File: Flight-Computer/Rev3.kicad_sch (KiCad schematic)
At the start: 2 parts, among them P11 440054-3, U14 MX25V5126FM1I

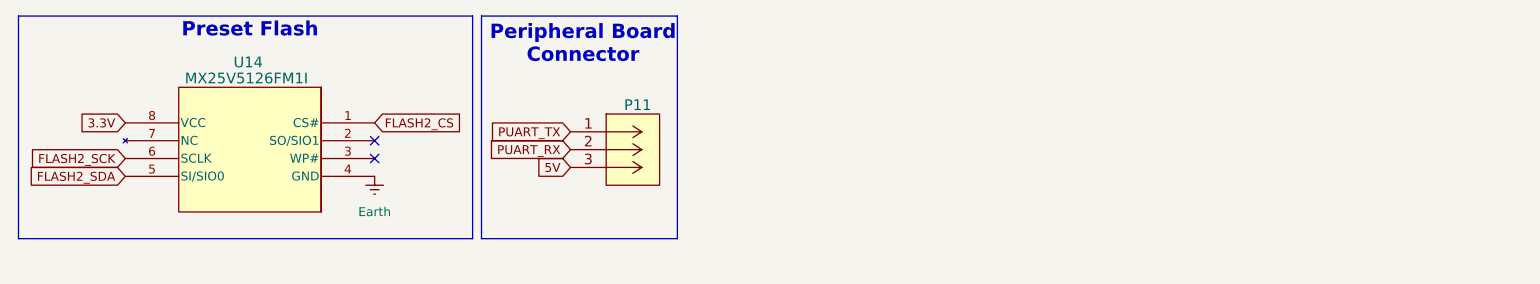
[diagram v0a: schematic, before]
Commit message: New Flash/4x UART
Added Microchip Technologies Flash and 3 more UART peripheral connectors
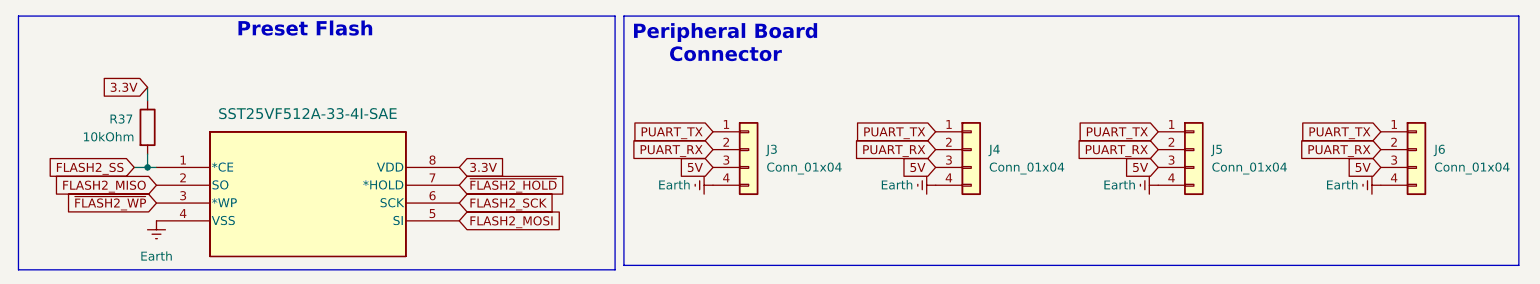
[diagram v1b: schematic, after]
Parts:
- removed P11: 440054-3, Flight-Computer:440054-3, symbol Flight-Computer:440054-3
- removed U14: MX25V5126FM1I, 8-SOP_MX25V_M1_MAC, symbol MX25V5126FM1I:MX25V5126FM1I
- added J3, J4, J5, J6: Conn_01x04, Connector_JST:JST_PH_B4B-PH-K_1x04_P2.00mm_Vertical, symbol Connector_Generic:Conn_01x04
- added R37: 10kOhm, symbol Device:R
- added U15: SST25VF512A-33-4I-SAE, SOIC8_SA_SST_MCH, symbol SST25VF512A-33-4I-SAE:SST25VF512A-33-4I-SAE
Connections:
- net 3.3V: now also R37.1, U15.8 (VDD)
- net 5V: now also J3.3 (Pin_3), J4.3 (Pin_3), J5.3 (Pin_3), J6.3 (Pin_3)
- net Earth: now also J3.4 (Pin_4), J4.4 (Pin_4), J5.4 (Pin_4), J6.4 (Pin_4), U15.4 (VSS)
- net FLASH2_SCK: now also U15.6 (SCK)
- net PUART_RX: now also J3.2 (Pin_2), J4.2 (Pin_2), J5.2 (Pin_2), J6.2 (Pin_2)
- net PUART_TX: now also J3.1 (Pin_1), J4.1 (Pin_1), J5.1 (Pin_1), J6.1 (Pin_1)
- new net FLASH2_MISO: U15.2 (SO)
- new net FLASH2_MOSI: U15.5 (SI)
- new net FLASH2_SS: R37.2, U15.1 (*CE)
- new net ~{FLASH2_HOLD}: U15.7 (*HOLD)
- new net ~{FLASH2_WP}: U15.3 (*WP)
- no-connect marks 2 -> 0

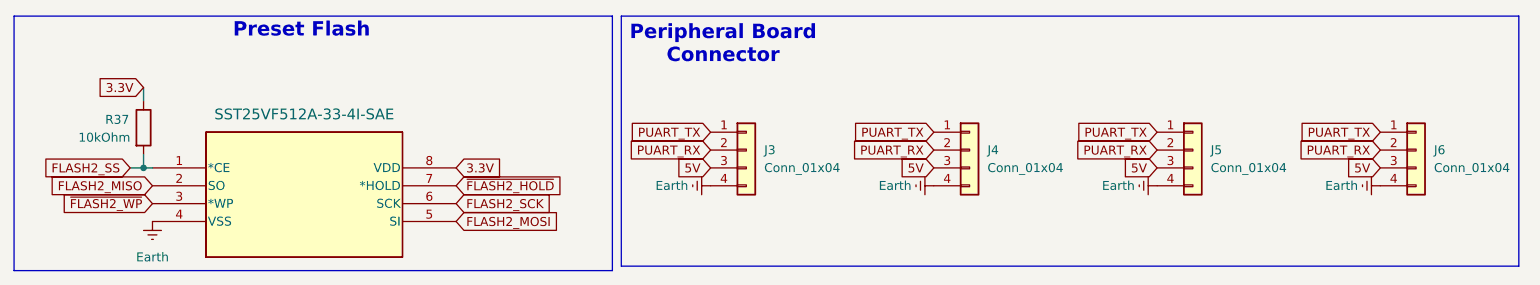
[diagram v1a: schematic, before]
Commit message: American PFLASH/PUART
Made to appease the American mind (Changed symbols and orientations)
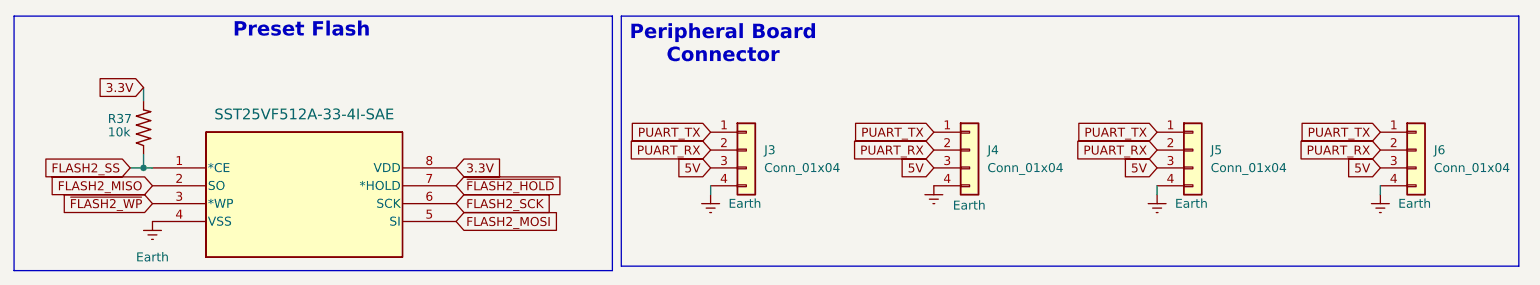
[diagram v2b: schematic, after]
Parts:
- removed R37: 10kOhm, symbol Device:R
- added R37: 10k, symbol Flight-Computer-Mac:RES_0603
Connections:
- net 3.3V: now also R37.2
- net FLASH2_SS: now also R37.1
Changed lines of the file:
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@@
+	(wire
+		(pts
+			(xy 111.76 38.1) (xy 111.76 36.83)
+		)
+		(stroke
+			(width 0)
+			(type default)
+		)
+	)
+	(wire
+		(pts
+			(xy 175.26 38.1) (xy 175.26 36.83)
+		)
+		(stroke
+			(width 0)
+			(type default)
+		)
+	)
 	(wire
 		(pts
@@
 		(pts
 			(xy 31.115 22.86) (xy 31.115 24.765)
+		)
+		(stroke
+			(width 0)
+			(type default)
+		)
+	)
+	(wire
+		(pts
+			(xy 207.01 38.1) (xy 207.01 36.83)
 		)
 		(stroke
@@
 	(symbol
 		(lib_id "power:Earth")
-		(at 175.26 36.83 270)
+		(at 175.26 38.1 0)
 		(unit 1)
 		(exclude_from_sim no)
@@
 		(fields_autoplaced yes)
 		(property "Reference" "#PWR067"
-			(at 168.91 36.83 0)
+			(at 175.26 44.45 0)
 			(effects
 				(font
@@
 		)
 		(property "Value" "Earth"
-			(at 172.085 36.8299 90)
-			(effects
-				(font
-					(size 1.27 1.27)
-				)
-				(justify right)
+			(at 177.8 39.3699 0)
+			(effects
+				(font
+					(size 1.27 1.27)
+				)
+				(justify left)
 			)
 		)
 		(property "Footprint" ""
-			(at 175.26 36.83 0)
+			(at 175.26 38.1 0)
 			(effects
 				(font
@@
 		)
 		(property "Datasheet" "~"
-			(at 175.26 36.83 0)
+			(at 175.26 38.1 0)
 			(effects
 				(font
@@
 		)
 		(property "Description" "Power symbol creates a global label with name \"Earth\""
-			(at 175.26 36.83 0)
+			(at 175.26 38.1 0)
 			(effects
 				(font
@@
 				(path "/15d2e012-e166-422c-a8f3-0484b565dd65/50820f75-73df-40b2-8569-4bcf15d0fdea"
 					(reference "#PWR067")
-					(unit 1)
-				)
-			)
-		)
-	)
-	(symbol
-		(lib_id "Device:R")
-		(at 31.115 28.575 0)
-		(unit 1)
-		(exclude_from_sim no)
-		(in_bom yes)
-		(on_board yes)
-		(dnp no)
-		(property "Reference" "R37"
-			(at 25.654 27.432 0)
-			(effects
-				(font
-					(size 1.27 1.27)
-				)
-				(justify left)
-			)
-		)
-		(property "Value" "10kOhm"
-			(at 21.844 29.972 0)
-			(effects
-				(font
-					(size 1.27 1.27)
-				)
-				(justify left)
-			)
-		)
-		(property "Footprint" ""
-			(at 29.337 28.575 90)
-			(effects
-				(font
-					(size 1.27 1.27)
-				)
-				(hide yes)
-			)
-		)
-		(property "Datasheet" "~"
-			(at 31.115 28.575 0)
-			(effects
-				(font
-					(size 1.27 1.27)
-				)
-				(hide yes)
-			)
-		)
-		(property "Description" "Resistor"
-			(at 31.115 28.575 0)
-			(effects
-				(font
-					(size 1.27 1.27)
-				)
-				(hide yes)
-			)
-		)
-		(pin "2"
-		)
-		(pin "1"
-		)
-		(instances
-			(project ""
-				(path "/15d2e012-e166-422c-a8f3-0484b565dd65/50820f75-73df-40b2-8569-4bcf15d0fdea"
-					(reference "R37")
 					(unit 1)
 				)
@@
 	(symbol
 		(lib_id "power:Earth")
-		(at 111.76 36.83 270)
+		(at 111.76 38.1 0)
 		(unit 1)
 		(exclude_from_sim no)
@@
 		(fields_autoplaced yes)
 		(property "Reference" "#PWR065"
-			(at 105.41 36.83 0)
+			(at 111.76 44.45 0)
 			(effects
 				(font
@@
 		)
 		(property "Value" "Earth"
-			(at 108.585 36.8299 90)
-			(effects
-				(font
-					(size 1.27 1.27)
-				)
-				(justify right)
+			(at 114.3 39.3699 0)
+			(effects
+				(font
+					(size 1.27 1.27)
+				)
+				(justify left)
 			)
 		)
 		(property "Footprint" ""
-			(at 111.76 36.83 0)
+			(at 111.76 38.1 0)
 			(effects
 				(font
@@
 		)
 		(property "Datasheet" "~"
-			(at 111.76 36.83 0)
+			(at 111.76 38.1 0)
 			(effects
 				(font
@@
 		)
 		(property "Description" "Power symbol creates a global label with name \"Earth\""
-			(at 111.76 36.83 0)
+			(at 111.76 38.1 0)
 			(effects
 				(font
@@
 				(path "/15d2e012-e166-422c-a8f3-0484b565dd65/50820f75-73df-40b2-8569-4bcf15d0fdea"
 					(reference "#PWR065")
+					(unit 1)
+				)
+			)
+		)
+	)
+	(symbol
+		(lib_id "Flight-Computer-Mac:RES_0603")
+		(at 31.115 28.575 90)
+		(unit 1)
+		(exclude_from_sim no)
+		(in_bom yes)
+		(on_board yes)
+		(dnp no)
+		(property "Reference" "R37"
+			(at 26.035 27.305 90)
+			(effects
+				(font
+					(size 1.27 1.27)
+				)
+				(justify right)
+			)
+		)
+		(property "Value" "10k"
+			(at 26.035 29.21 90)
+			(effects
+				(font
+					(size 1.27 1.27)
+				)
+				(justify right)
+			)
+		)
+		(property "Footprint" ""
+			(at 43.815 27.305 0)
+			(effects
+				(font
+					(size 1.27 1.27)
+				)
+				(justify left bottom)
+				(hide yes)
+			)
+		)
+		(property "Datasheet" ""
+			(at 31.115 28.575 0)
+			(effects
+				(font
+					(size 1.27 1.27)
+				)
+				(justify left bottom)
+				(hide yes)
+			)
+		)
+		(property "Description" ""
+			(at 31.115 28.575 0)
+			(effects
+				(font
+					(size 1.27 1.27)
+				)
+				(hide yes)
+			)
+		)
+		(pin "1"
+		)
+		(pin "2"
+		)
+		(instances
+			(project ""
+				(path "/15d2e012-e166-422c-a8f3-0484b565dd65/50820f75-73df-40b2-8569-4bcf15d0fdea"
+					(reference "R37")
 					(unit 1)
 				)
@@
 	(symbol
 		(lib_id "power:Earth")
-		(at 207.01 36.83 270)
+		(at 207.01 38.1 0)
 		(unit 1)
 		(exclude_from_sim no)
@@
 		(fields_autoplaced yes)
 		(property "Reference" "#PWR068"
-			(at 200.66 36.83 0)
+			(at 207.01 44.45 0)
 			(effects
 				(font
@@
 		)
 		(property "Value" "Earth"
-			(at 203.835 36.8299 90)
-			(effects
-				(font
-					(size 1.27 1.27)
-				)
-				(justify right)
+			(at 209.55 39.3699 0)
+			(effects
+				(font
+					(size 1.27 1.27)
+				)
+				(justify left)
 			)
 		)
 		(property "Footprint" ""
-			(at 207.01 36.83 0)
+			(at 207.01 38.1 0)
 			(effects
 				(font
@@
 		)
 		(property "Datasheet" "~"
-			(at 207.01 36.83 0)
+			(at 207.01 38.1 0)
 			(effects
 				(font
@@
 		)
 		(property "Description" "Power symbol creates a global label with name \"Earth\""
-			(at 207.01 36.83 0)
+			(at 207.01 38.1 0)
 			(effects
 				(font
@@
 	(symbol
 		(lib_id "power:Earth")
-		(at 143.51 36.83 270)
+		(at 143.51 36.83 0)
 		(unit 1)
 		(exclude_from_sim no)
@@
 		(on_board yes)
 		(dnp no)
-		(fields_autoplaced yes)
 		(property "Reference" "#PWR066"
-			(at 137.16 36.83 0)
+			(at 143.51 43.18 0)
 			(effects
 				(font
@@
 		)
 		(property "Value" "Earth"
-			(at 140.335 36.8299 90)
-			(effects
-				(font
+			(at 150.876 39.624 0)
+			(effects
+				(font

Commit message: Update Rev3.kicad_sch
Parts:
- removed R37: 10k, symbol Flight-Computer-Mac:RES_0603
- added R37: 10k, Flight-Computer:RES_0603, symbol Flight-Computer:RES_0603
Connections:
- net 3.3V: now also R37.2
- net FLASH2_SS: now also R37.1
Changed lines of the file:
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@@
 	)
 	(symbol
-		(lib_id "Flight-Computer-Mac:RES_0603")
+		(lib_id "Flight-Computer:RES_0603")
 		(at 31.115 28.575 90)
 		(unit 1)
@@
 		(on_board yes)
 		(dnp no)
+		(fields_autoplaced yes)
 		(property "Reference" "R37"
-			(at 26.035 27.305 90)
+			(at 32.8676 27.7403 90)
 			(effects
 				(font
@@
 		)
 		(property "Value" "10k"
-			(at 26.035 29.21 90)
+			(at 32.8676 30.2772 90)
 			(effects
 				(font
@@
 			)
 		)
-		(property "Footprint" ""
+		(property "Footprint" "Flight-Computer:RES_0603"
 			(at 43.815 27.305 0)
 			(effects
@@
 		)
 		(instances
-			(project ""
+			(project "Flight-Computer"
 				(path "/15d2e012-e166-422c-a8f3-0484b565dd65/50820f75-73df-40b2-8569-4bcf15d0fdea"
 					(reference "R37")

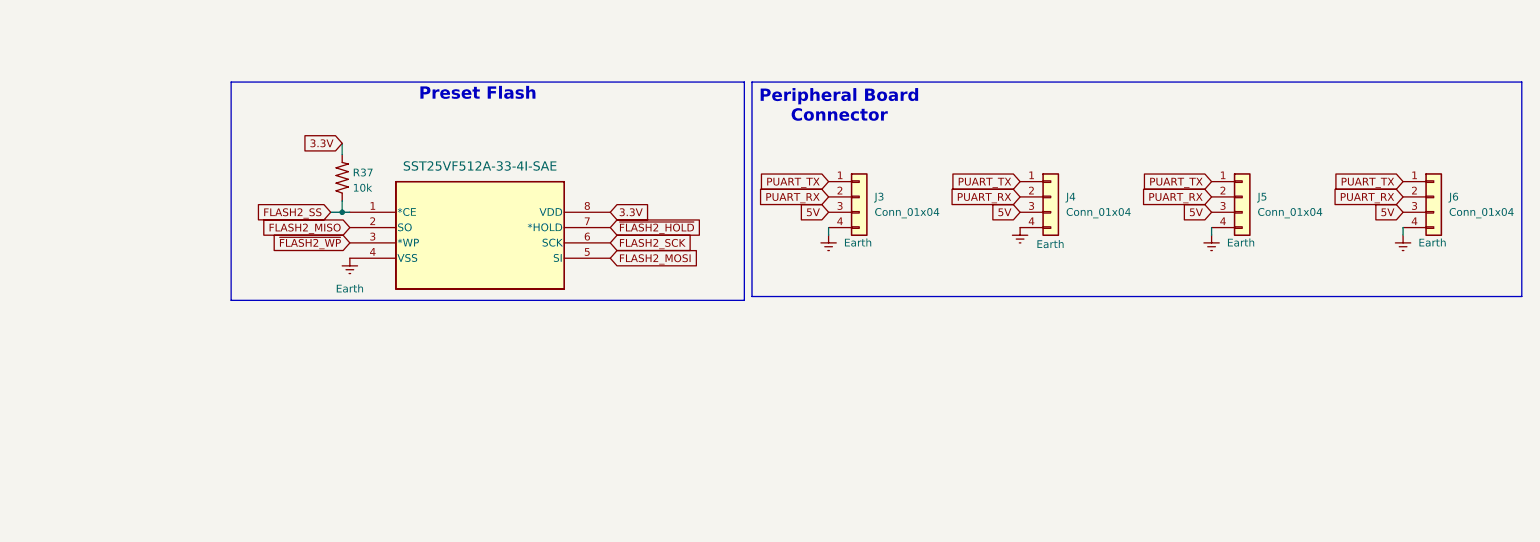
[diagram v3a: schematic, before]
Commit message: Ports
Added 2 UART ports for connectivity, expanded board
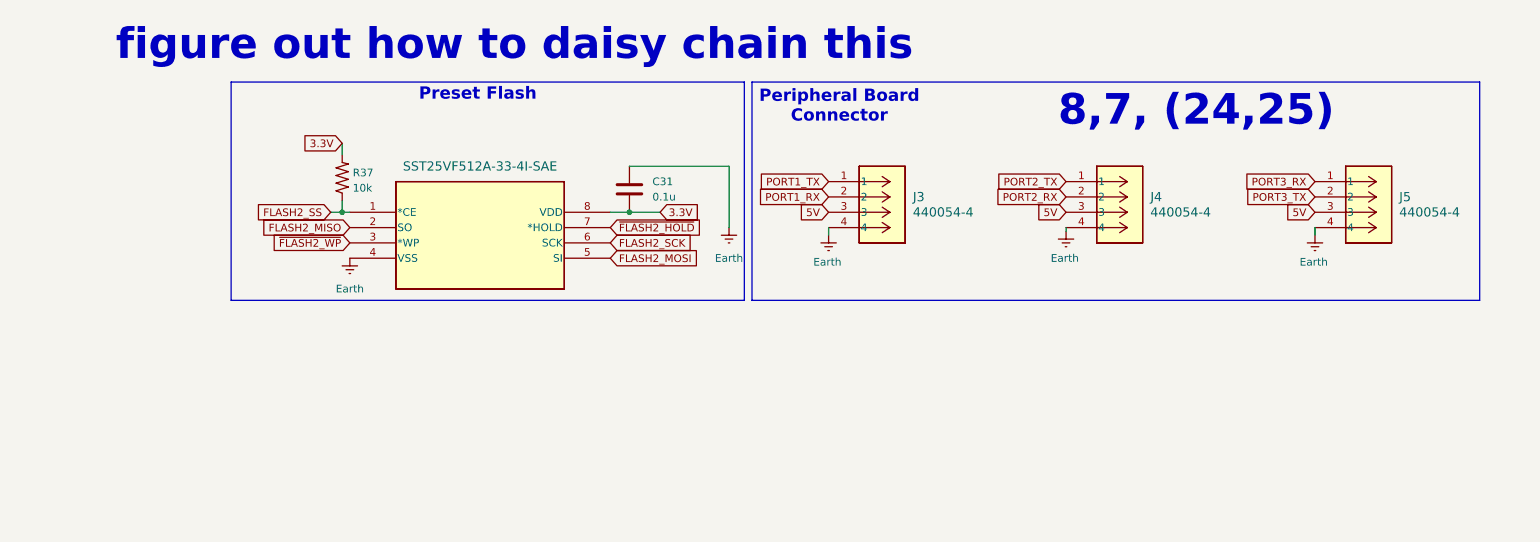
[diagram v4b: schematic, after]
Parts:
- removed J3, J4, J5, J6: Conn_01x04, Connector_JST:JST_PH_B4B-PH-K_1x04_P2.00mm_Vertical, symbol Connector_Generic:Conn_01x04
- added C31: 0.1u, Capacitor_SMD:C_0603_1608Metric, symbol Device:C
- added J3, J4, J5: 440054-4, 440054_4:CONN_440054-4_TEC, symbol 2025-03-27_16-40-08:440054-4
- R37: footprint Flight-Computer:RES_0603 -> Flight-Computer-Mac:RES_0603
- U15: footprint SOIC8_SA_SST_MCH -> SST25:SOIC8_SA_SST_MCH
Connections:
- net 3.3V: now also C31.2
- net 5V: now also J3.3, J4.3, J5.3
- net Earth: now also C31.1, J3.4, J4.4, J5.4
- new net PORT1_RX: J3.2
- new net PORT1_TX: J3.1
- new net PORT2_RX: J4.2
- new net PORT2_TX: J4.1
- new net PORT3_RX: J5.1
- new net PORT3_TX: J5.2
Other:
- note added: "8,7, (24,25)"
- note added: "figure out how to daisy chain this"

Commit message: most up to date rev 2.5 files
third connector (where micro sd used to be) does not have tx3 pins connected (pin outs needed in order to wire)
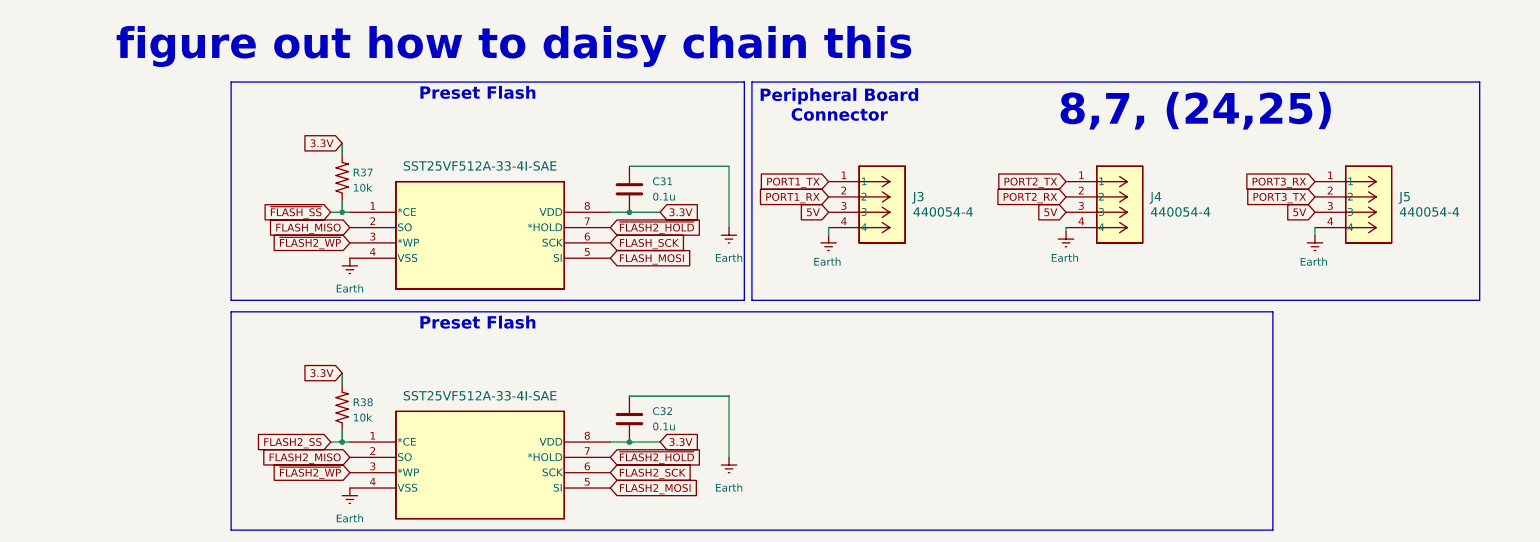
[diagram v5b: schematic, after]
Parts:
- added C32: 0.1u, Capacitor_SMD:C_0603_1608Metric, symbol Device:C
- added R38: 10k, Flight-Computer-Mac:RES_0603, symbol Flight-Computer:RES_0603
- added U14: SST25VF512A-33-4I-SAE, SST25:SOIC8_SA_SST_MCH, symbol SST25VF512A-33-4I-SAE:SST25VF512A-33-4I-SAE
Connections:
- net 3.3V: now also C32.2, R38.2, U14.8 (VDD)
- net Earth: now also C32.1, U14.4 (VSS)
- net FLASH2_MISO: now also U14.2 (SO); no longer U15.2 (SO)
- net FLASH2_MOSI: now also U14.5 (SI); no longer U15.5 (SI)
- net FLASH2_SCK: now also U14.6 (SCK); no longer U15.6 (SCK)
- net FLASH2_SS: now also R38.1, U14.1 (*CE); no longer R37.1, U15.1 (*CE)
- net ~{FLASH2_HOLD}: now also U14.7 (*HOLD)
- net ~{FLASH2_WP}: now also U14.3 (*WP)
- new net FLASH_MISO: U15.2 (SO)
- new net FLASH_MOSI: U15.5 (SI)
- new net FLASH_SCK: U15.6 (SCK)
- new net ~{FLASH_SS}: R37.1, U15.1 (*CE)
